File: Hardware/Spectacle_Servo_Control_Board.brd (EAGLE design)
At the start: 25.4 x 55.9 mm, 39 parts, among them J1 FTDI_DEVICE, J10 AUDIO-JACK3, J3 USB-MICROB, J4 AUDIO-JACK3, U1 CY8C4146LQI-S422, U2 3.3V/150mA

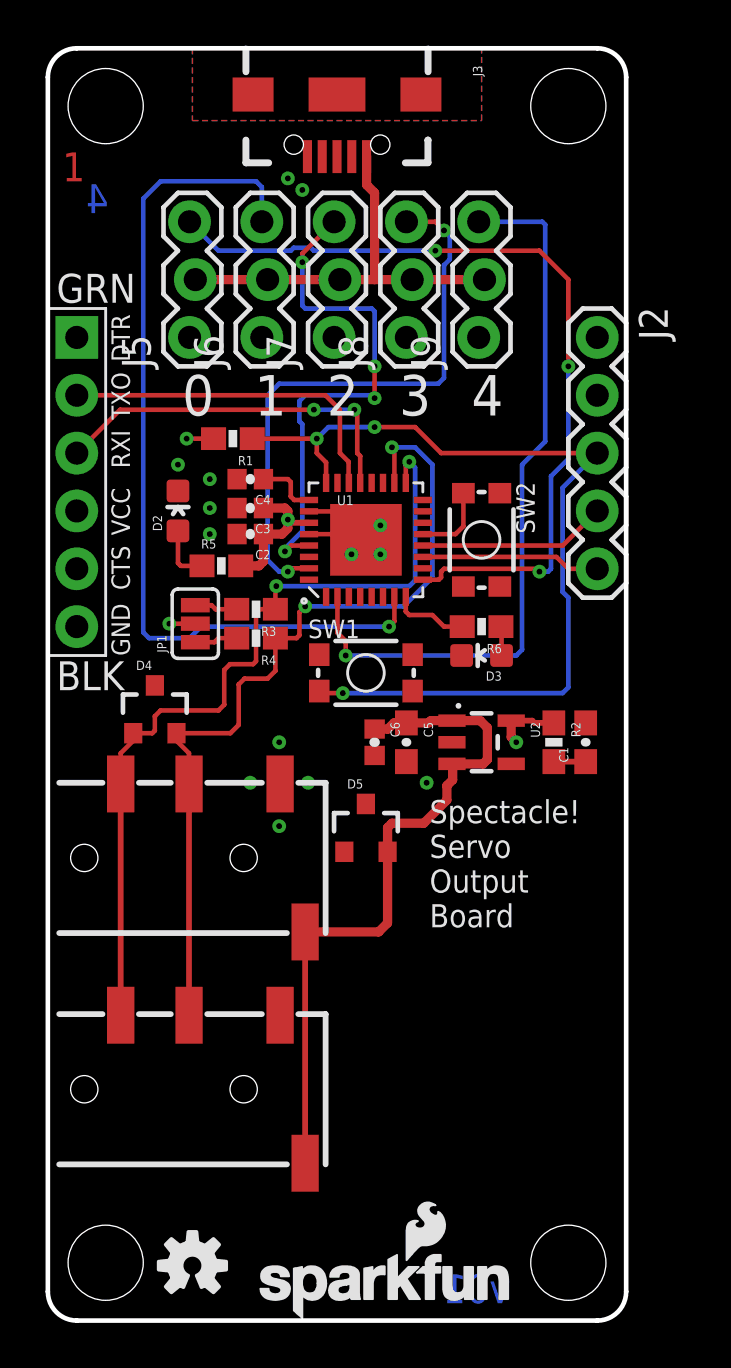
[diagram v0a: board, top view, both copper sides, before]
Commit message: Changes from design review, initial checklist pass
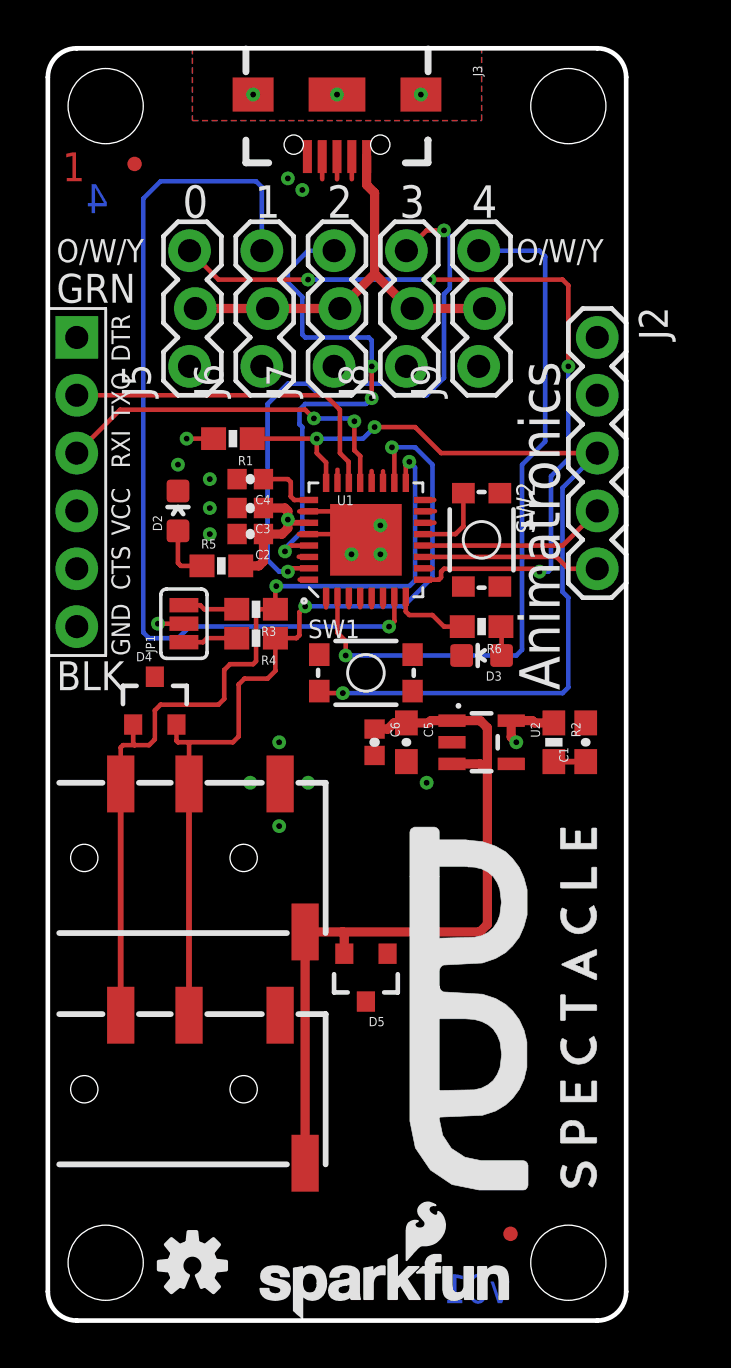
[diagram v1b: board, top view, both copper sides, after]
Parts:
- added FD1, FD2: FIDUCIALUFIDUCIAL, SparkFun-Aesthetics:MICRO-FIDUCIAL
- added LOGO3: SFE_LOGO_NAME_FLAME.1_INCH, SparkFun-Aesthetics:SFE_LOGO_NAME_FLAME_.1
- added LOGO4: OSHW-LOGOS, SparkFun-Aesthetics:OSHW-LOGO-S
- added U$2: (no value), SparkFun-Aesthetics:SPECTACLE_LOGO_TITLE_0.35X0.70
- added U$3: (no value), SparkFun-Aesthetics:SPECTACLE_LOGO_NEGATIVE_1.5X0.5
- D3: value RED -> Yellow
- moved D5 6.48 mm to (14.0, 15.1), turned to 180 degrees
- moved J5 1.27 mm to (6.35, 41.9)
- moved J6 1.27 mm to (9.53, 41.9)
- moved J7 1.27 mm to (12.7, 41.9)
- moved J8 1.27 mm to (15.9, 41.9)
- moved J9 1.27 mm to (19.1, 41.9)
- moved JP1 0.50 mm to (5.98, 30.6)
- moved D4 0.38 mm to (4.70, 27.2)
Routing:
- net VIN: track 31.2 -> 34.9 mm
- net SERVO_4: track 32.6 -> 31.3 mm
- net SERVO_1: track 38.7 -> 40.0 mm
- net SCL: track 37.2 -> 38.3 mm
- net 5V: track 18.2 -> 19.3 mm
- net SERVO_3: track 25.9 -> 26.7 mm
- net SERVO_0: track 36.9 -> 36.1 mm, vias 3 -> 4
- net N$1: track 0.00 -> 0.72 mm
- net N$7: track 0.00 -> 0.60 mm
- net SDA: track 37.9 -> 38.5 mm
- net N$8: track 0.00 -> 0.58 mm
- net N$6: track 1.89 -> 2.39 mm
- net N$24: track 0.00 -> 0.50 mm
- net N$23: track 0.00 -> 0.50 mm
- net N$22: track 0.00 -> 0.50 mm
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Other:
- board text added: "Animatronics"
- board text added: "O/W/Y"
- board text removed: "Spectacle\! Servo Output Board"

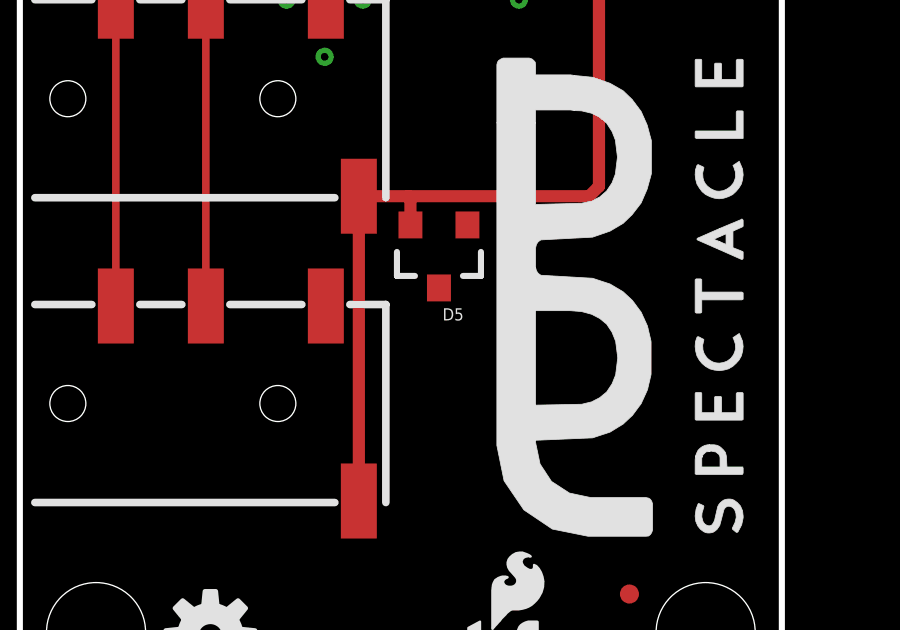
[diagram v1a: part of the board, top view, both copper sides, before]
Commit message: Revised from feedback from QC
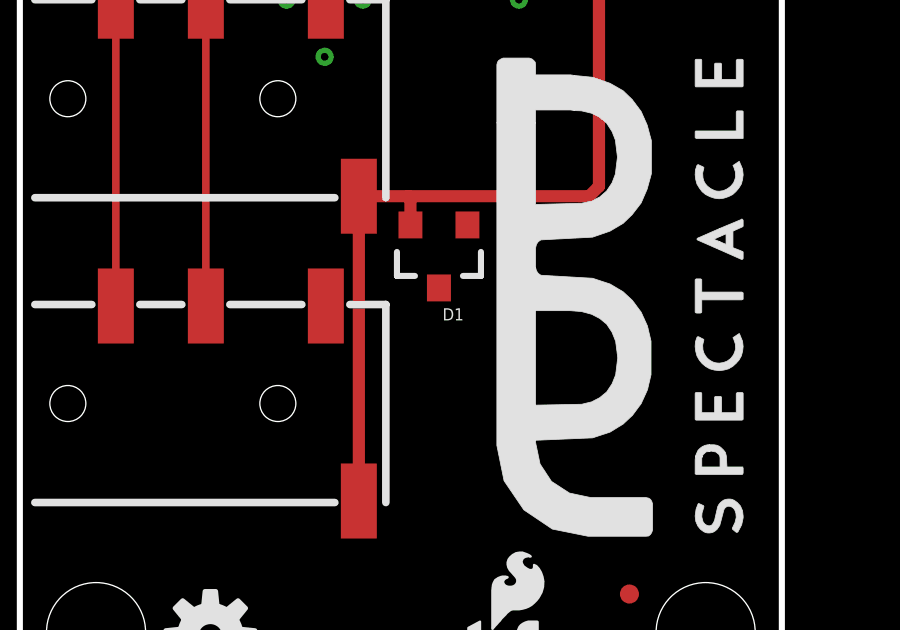
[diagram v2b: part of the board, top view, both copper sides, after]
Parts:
- renumbered D5 to D1
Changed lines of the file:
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@@
 <layers>
 <layer number="1" name="Top" color="4" fill="1" visible="yes" active="yes"/>
-<layer number="2" name="Route2" color="1" fill="3" visible="yes" active="yes"/>
-<layer number="15" name="Route15" color="4" fill="6" visible="yes" active="yes"/>
+<layer number="2" name="Route2" color="1" fill="3" visible="no" active="yes"/>
+<layer number="15" name="Route15" color="4" fill="6" visible="no" active="yes"/>
 <layer number="16" name="Bottom" color="1" fill="1" visible="yes" active="yes"/>
 <layer number="17" name="Pads" color="2" fill="1" visible="yes" active="yes"/>
@@
 <layer number="23" name="tOrigins" color="15" fill="1" visible="yes" active="yes"/>
 <layer number="24" name="bOrigins" color="15" fill="1" visible="yes" active="yes"/>
-<layer number="25" name="tNames" color="7" fill="1" visible="yes" active="yes"/>
-<layer number="26" name="bNames" color="7" fill="1" visible="yes" active="yes"/>
-<layer number="27" name="tValues" color="7" fill="1" visible="yes" active="yes"/>
-<layer number="28" name="bValues" color="7" fill="1" visible="yes" active="yes"/>
-<layer number="29" name="tStop" color="7" fill="3" visible="yes" active="yes"/>
-<layer number="30" name="bStop" color="7" fill="6" visible="yes" active="yes"/>
-<layer number="31" name="tCream" color="7" fill="4" visible="yes" active="yes"/>
-<layer number="32" name="bCream" color="7" fill="5" visible="yes" active="yes"/>
-<layer number="39" name="tKeepout" color="4" fill="11" visible="yes" active="yes"/>
-<layer number="40" name="bKeepout" color="1" fill="11" visible="yes" active="yes"/>
-<layer number="41" name="tRestrict" color="4" fill="10" visible="yes" active="yes"/>
-<layer number="42" name="bRestrict" color="1" fill="10" visible="yes" active="yes"/>
-<layer number="43" name="vRestrict" color="2" fill="10" visible="yes" active="yes"/>
-<layer number="44" name="Drills" color="7" fill="1" visible="yes" active="yes"/>
+<layer number="25" name="tNames" color="7" fill="1" visible="no" active="yes"/>
+<layer number="26" name="bNames" color="7" fill="1" visible="no" active="yes"/>
+<layer number="27" name="tValues" color="7" fill="1" visible="no" active="yes"/>
+<layer number="28" name="bValues" color="7" fill="1" visible="no" active="yes"/>
+<layer number="29" name="tStop" color="7" fill="3" visible="no" active="yes"/>
+<layer number="30" name="bStop" color="7" fill="6" visible="no" active="yes"/>
+<layer number="31" name="tCream" color="7" fill="4" visible="no" active="yes"/>
+<layer number="32" name="bCream" color="7" fill="5" visible="no" active="yes"/>
+<layer number="39" name="tKeepout" color="4" fill="11" visible="no" active="yes"/>
+<layer number="40" name="bKeepout" color="1" fill="11" visible="no" active="yes"/>
+<layer number="41" name="tRestrict" color="4" fill="10" visible="no" active="yes"/>
+<layer number="42" name="bRestrict" color="1" fill="10" visible="no" active="yes"/>
+<layer number="43" name="vRestrict" color="2" fill="10" visible="no" active="yes"/>
+<layer number="44" name="Drills" color="7" fill="1" visible="no" active="yes"/>
 <layer number="45" name="Holes" color="7" fill="1" visible="yes" active="yes"/>
-<layer number="46" name="Milling" color="3" fill="1" visible="yes" active="yes"/>
-<layer number="47" name="Measures" color="7" fill="1" visible="yes" active="yes"/>
+<layer number="46" name="Milling" color="3" fill="1" visible="no" active="yes"/>
+<layer number="47" name="Measures" color="7" fill="1" visible="no" active="yes"/>
 <layer number="51" name="tDocu" color="6" fill="1" visible="yes" active="yes"/>
-<layer number="52" name="bDocu" color="7" fill="1" visible="yes" active="yes"/>
+<layer number="52" name="bDocu" color="7" fill="1" visible="no" active="yes"/>
 <layer number="3" name="Route3" color="4" fill="3" visible="no" active="no"/>
 <layer number="4" name="Route4" color="1" fill="4" visible="no" active="no"/>
@@
 <attribute name="PROD_ID" value="RES-07856" x="19.05" y="30.48" size="1.778" layer="27" font="vector" ratio="15" rot="R180" display="off"/>
 </element>
-<element name="J4" library="SparkFun-Connectors" package="AUDIO-JACK-TRRS-SMD" value="AUDIO-JACK3" x="0" y="20.32"/>
+<element name="J4" library="SparkFun-Connectors" package="AUDIO-JACK-TRRS-SMD" value="AUDIO-JACK3" x="0" y="20.32">
+<attribute name="PROD_ID" value="CONN-10676" x="0" y="20.32" size="1.778" layer="27" display="off"/>
+</element>
 <element name="D4" library="SparkFun-DiscreteSemi" package="SOT23-3" value="PESD1CAN" x="4.699" y="27.178">
 <attribute name="PROD_ID" value="DIO-12501" x="4.699" y="27.178" size="1.778" layer="27" font="vector" ratio="15" display="off"/>
 </element>
-<element name="D5" library="SparkFun-DiscreteSemi" package="SOT23-3" value="PESD1CAN" x="13.97" y="15.113" rot="R180">
+<element name="D1" library="SparkFun-DiscreteSemi" package="SOT23-3" value="PESD1CAN" x="13.97" y="15.113" rot="R180">
 <attribute name="PROD_ID" value="DIO-12501" x="13.97" y="15.113" size="1.778" layer="27" font="vector" ratio="15" rot="R180" display="off"/>
 </element>
@@
 <element name="LOGO1" library="SparkFun-Aesthetics" package="OSHW-LOGO-S" value="OSHW-LOGOS" x="6.35" y="2.413"/>
 <element name="LOGO2" library="SparkFun-Aesthetics" package="SFE_LOGO_NAME_FLAME_.1" value="SFE_LOGO_NAME_FLAME.1_INCH" x="8.89" y="0"/>
-<element name="J10" library="SparkFun-Connectors" package="AUDIO-JACK-TRRS-SMD" value="AUDIO-JACK3" x="0" y="10.16"/>
+<element name="J10" library="SparkFun-Connectors" package="AUDIO-JACK-TRRS-SMD" value="AUDIO-JACK3" x="0" y="10.16">
+<attribute name="PROD_ID" value="CONN-10676" x="0" y="10.16" size="1.778" layer="27" display="off"/>
+</element>
 <element name="U$2" library="SparkFun-Aesthetics" package="SPECTACLE_LOGO_TITLE_0.35X0.70" value="" x="24.13" y="5.715" rot="R90"/>
 <element name="LOGO3" library="SparkFun-Aesthetics" package="SFE_LOGO_NAME_FLAME_.1" value="SFE_LOGO_NAME_FLAME.1_INCH" x="0.762" y="4.445" rot="MR90"/>
@@
 <contactref element="J4" pad="TIP"/>
 <contactref element="D4" pad="3"/>
-<contactref element="D5" pad="3"/>
+<contactref element="D1" pad="3"/>
 <polygon width="0.2032" layer="1" isolate="0.3048" rank="2">
 <vertex x="0" y="1.27"/>
@@
 <wire x1="16.725" y1="26.25" x2="16.825" y2="26.35" width="0.4064" layer="1"/>
 <wire x1="16.825" y1="26.35" x2="17.7499" y2="26.35" width="0.4064" layer="1"/>
-<contactref element="D5" pad="2"/>
+<contactref element="D1" pad="2"/>
 <wire x1="17.78" y1="24.4199" x2="17.7499" y2="24.45" width="0.4064" layer="1"/>
 <wire x1="19.304" y1="26.035" x2="18.989" y2="26.35" width="0.4064" layer="1"/>

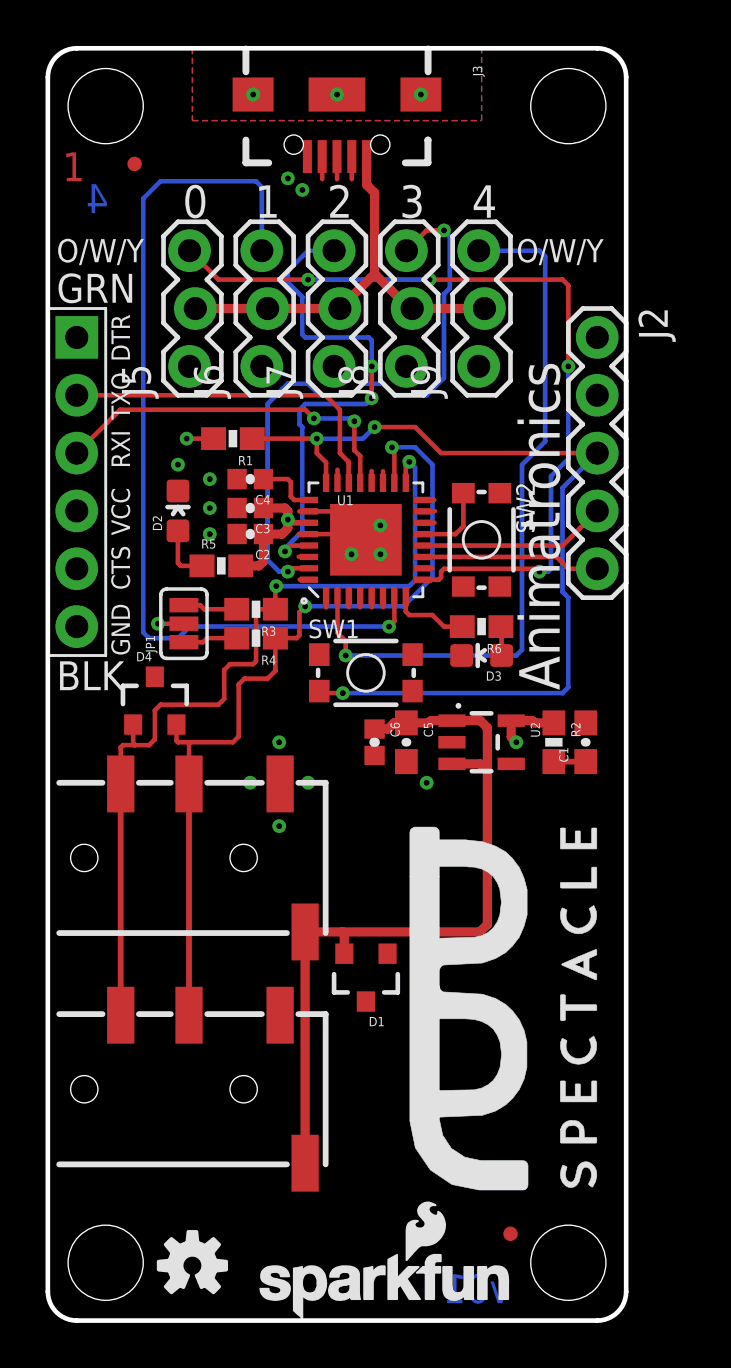
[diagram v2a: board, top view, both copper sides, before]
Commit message: Added downstream power control circuitry
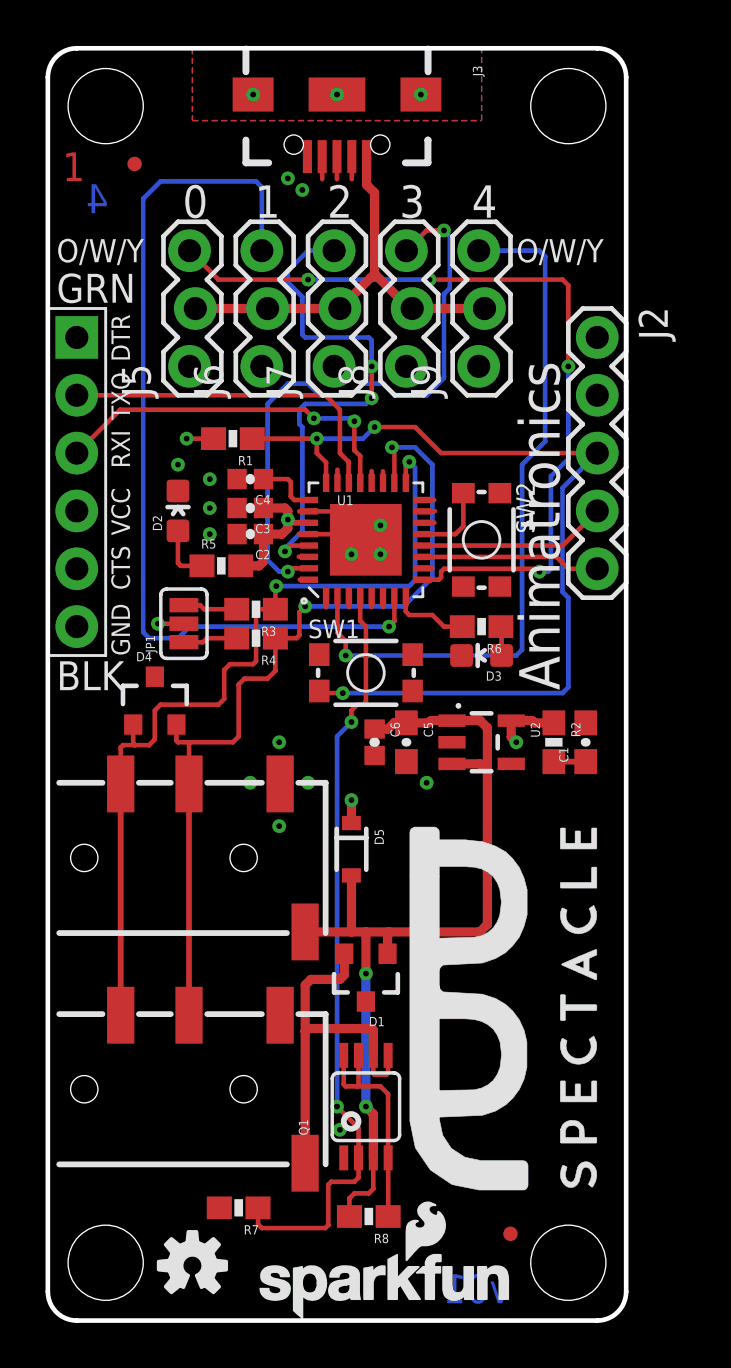
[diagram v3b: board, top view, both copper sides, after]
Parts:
- added D5: BAT20J, SparkFun-DiscreteSemi:SOD-323
- added Q1: (no value), SparkFun-DiscreteSemi:MSOP8
- added R7, R8: 10K, SparkFun-Resistors:0603-RES
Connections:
- new net N$26: Q1.4, Q1.7, Q1.8, R8.1
- new net VOUT: D1.2, J10.EARTH, Q1.5, Q1.6
- new net V_OUT_EN: Q1.2, R7.1, U1.4
- net 5V: now also D5.C
- net GND: now also Q1.1, R7.2
- net VIN: now also D1.1, D5.A, Q1.3, R8.2; no longer D1.2, J10.EARTH
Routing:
- net V_OUT_EN: track 0.00 -> 33.8 mm, vias 0 -> 2
- net 5V: track 19.3 -> 43.8 mm, vias 0 -> 1
- net VOUT: track 0.00 -> 18.3 mm
- net N$26: track 0.00 -> 10.2 mm
- net VIN: track 34.9 -> 40.6 mm, vias 0 -> 2
- net N$18: track 0.50 -> 0.00 mm
- net GND: vias 14 -> 15
